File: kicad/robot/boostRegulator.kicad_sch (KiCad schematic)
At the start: 22 parts, among them U5 LSF0102DCTR, U6 MAX77857

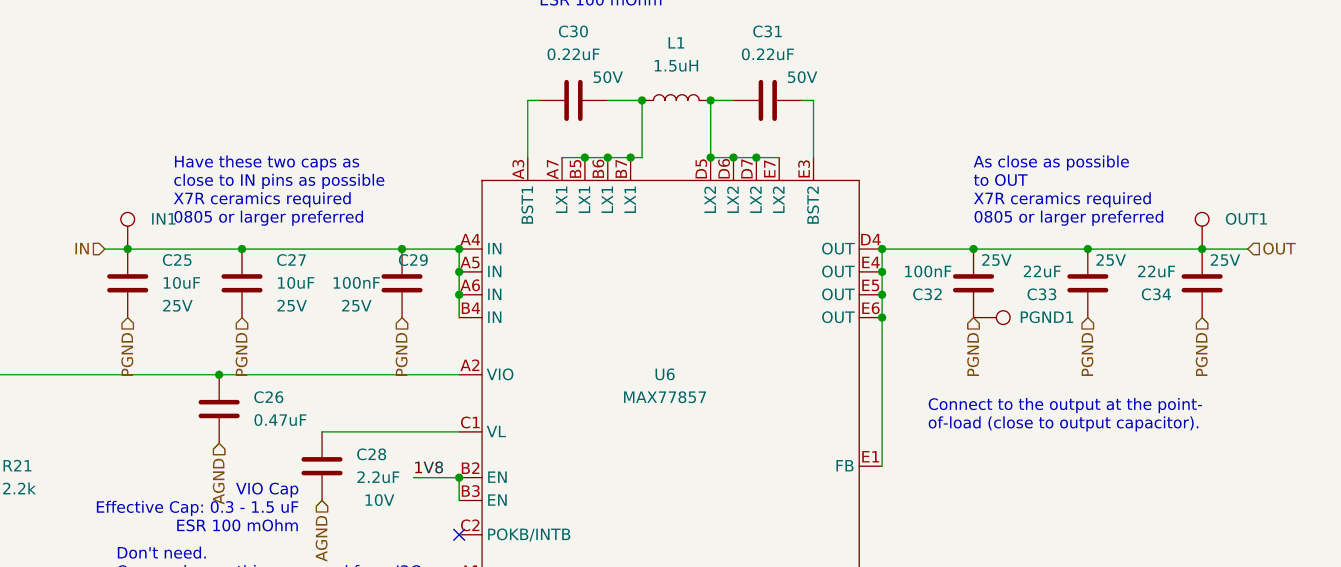
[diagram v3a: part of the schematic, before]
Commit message: Assigned capacitor footprints
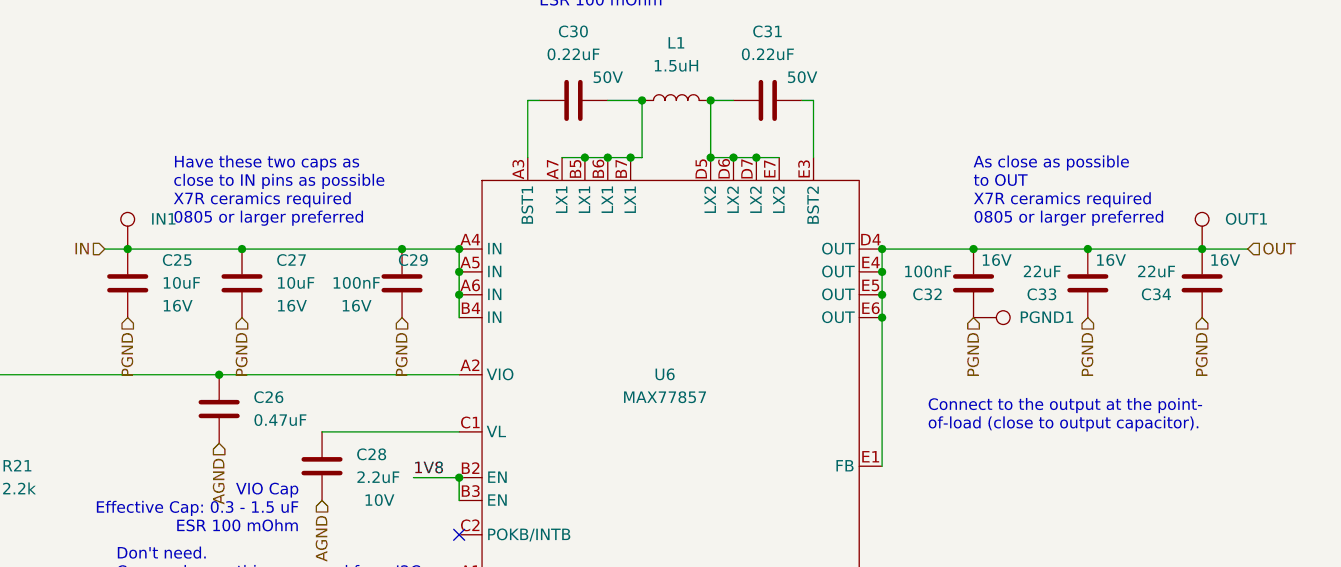
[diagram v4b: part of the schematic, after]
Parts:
- C24, C26, C28, C30, C31: footprint (none) -> Capacitor_SMD:C_0603_1608Metric
- C25, C27, C29, C32, C33, C34: footprint (none) -> Capacitor_SMD:C_0805_2012Metric
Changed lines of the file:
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@@
       (effects (font (size 1.27 1.27)) (justify left))
     )
-    (property "Footprint" "" (id 2) (at 157.1752 118.11 0)
+    (property "Footprint" "Capacitor_SMD:C_0603_1608Metric" (id 2) (at 157.1752 118.11 0)
       (effects (font (size 1.27 1.27)) hide)
     )
@@
     (property "Reference" "C32" (id 0) (at 223.52 95.25 0))
     (property "Value" "100nF" (id 1) (at 223.52 92.71 0))
-    (property "Footprint" "" (id 2) (at 227.6348 90.17 0)
+    (property "Footprint" "Capacitor_SMD:C_0805_2012Metric" (id 2) (at 227.6348 90.17 0)
       (effects (font (size 1.27 1.27)) hide)
     )
@@
       (effects (font (size 1.27 1.27)) hide)
     )
-    (property "Description" "25V" (id 4) (at 231.14 91.44 0))
+    (property "Description" "16V" (id 4) (at 231.14 91.44 0))
     (pin "1")
     (pin "2")
@@
       (effects (font (size 1.27 1.27)) (justify left))
     )
-    (property "Footprint" "" (id 2) (at 148.2852 97.79 0)
+    (property "Footprint" "Capacitor_SMD:C_0805_2012Metric" (id 2) (at 148.2852 97.79 0)
       (effects (font (size 1.27 1.27)) hide)
     )
@@
       (effects (font (size 1.27 1.27)) hide)
     )
-    (property "Description" "25V" (id 4) (at 151.13 96.5199 0)
+    (property "Description" "16V" (id 4) (at 151.13 96.5199 0)
       (effects (font (size 1.27 1.27)) (justify left))
     )
@@
       (effects (font (size 1.27 1.27)) (justify left))
     )
-    (property "Footprint" "" (id 2) (at 135.5852 97.79 0)
+    (property "Footprint" "Capacitor_SMD:C_0805_2012Metric" (id 2) (at 135.5852 97.79 0)
       (effects (font (size 1.27 1.27)) hide)
     )
@@
       (effects (font (size 1.27 1.27)) hide)
     )
-    (property "Description" "25V" (id 4) (at 138.43 96.5199 0)
+    (property "Description" "16V" (id 4) (at 138.43 96.5199 0)
       (effects (font (size 1.27 1.27)) (justify left))
     )
@@
       (effects (font (size 1.27 1.27)) (justify left))
     )
-    (property "Footprint" "" (id 2) (at 45.4152 124.46 0)
+    (property "Footprint" "Capacitor_SMD:C_0603_1608Metric" (id 2) (at 45.4152 124.46 0)
       (effects (font (size 1.27 1.27)) hide)
     )
@@
     (property "Reference" "C29" (id 0) (at 166.37 91.44 0))
     (property "Value" "100nF" (id 1) (at 160.02 93.98 0))
-    (property "Footprint" "" (id 2) (at 164.1348 90.17 0)
+    (property "Footprint" "Capacitor_SMD:C_0805_2012Metric" (id 2) (at 164.1348 90.17 0)
       (effects (font (size 1.27 1.27)) hide)
     )
@@
       (effects (font (size 1.27 1.27)) hide)
     )
-    (property "Description" "25V" (id 4) (at 160.02 96.52 0))
+    (property "Description" "16V" (id 4) (at 160.02 96.52 0))
     (pin "1")
     (pin "2")
@@
     (property "Reference" "C34" (id 0) (at 248.92 95.25 0))
     (property "Value" "22uF" (id 1) (at 248.92 92.71 0))
-    (property "Footprint" "" (id 2) (at 253.0348 90.17 0)
+    (property "Footprint" "Capacitor_SMD:C_0805_2012Metric" (id 2) (at 253.0348 90.17 0)
       (effects (font (size 1.27 1.27)) hide)
     )
@@
       (effects (font (size 1.27 1.27)) hide)
     )
-    (property "Description" "25V" (id 4) (at 256.54 91.44 0))
+    (property "Description" "16V" (id 4) (at 256.54 91.44 0))
     (pin "1")
     (pin "2")
@@
     (property "Reference" "C33" (id 0) (at 236.22 95.25 0))
     (property "Value" "22uF" (id 1) (at 236.22 92.71 0))
-    (property "Footprint" "" (id 2) (at 240.3348 90.17 0)
+    (property "Footprint" "Capacitor_SMD:C_0805_2012Metric" (id 2) (at 240.3348 90.17 0)
       (effects (font (size 1.27 1.27)) hide)
     )
@@
       (effects (font (size 1.27 1.27)) hide)
     )
-    (property "Description" "25V" (id 4) (at 243.84 91.44 0))
+    (property "Description" "16V" (id 4) (at 243.84 91.44 0))
     (pin "1")
     (pin "2")
@@
     (property "Reference" "C30" (id 0) (at 184.15 66.04 90))
     (property "Value" "0.22uF" (id 1) (at 184.15 68.58 90))
-    (property "Footprint" "" (id 2) (at 187.96 72.6948 0)
+    (property "Footprint" "Capacitor_SMD:C_0603_1608Metric" (id 2) (at 187.96 72.6948 0)
       (effects (font (size 1.27 1.27)) hide)
     )
@@
       (effects (font (size 1.27 1.27)) (justify left))
     )
-    (property "Footprint" "" (id 2) (at 145.7452 111.76 0)
+    (property "Footprint" "Capacitor_SMD:C_0603_1608Metric" (id 2) (at 145.7452 111.76 0)
       (effects (font (size 1.27 1.27)) hide)
     )
@@
     (property "Reference" "C31" (id 0) (at 205.74 66.04 90))
     (property "Value" "0.22uF" (id 1) (at 205.74 68.58 90))
-    (property "Footprint" "" (id 2) (at 209.55 72.6948 0)
-      (effects (font (size 1.27 1.27)) hide)
-    )
+    (property "Footprint" "Capacitor_SMD:C_0603_1608Metric" (id 2) (at 209.55 72.6948 0)
+      (effects (font (size 1.27 1.27)) hide)
+    )

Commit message: Added IND_TAIYO_NRS6028_TAY footprint and model to boost
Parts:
- L1: footprint (none) -> custom_inductors:NRS6028T1R5NMGJ; Manufacturer (none) -> TAIYO YUDEN; Part Number CDMT40D20HF-1R5NC -> NRS6028T1R5NMGJ
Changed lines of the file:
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@@
     (property "Reference" "L1" (id 0) (at 195.58 67.31 90))
     (property "Value" "1.5uH" (id 1) (at 195.58 69.85 90))
-    (property "Footprint" "" (id 2) (at 195.58 73.66 0)
+    (property "Footprint" "custom_inductors:NRS6028T1R5NMGJ" (id 2) (at 195.58 73.66 0)
       (effects (font (size 1.27 1.27)) hide)
     )
-    (property "Datasheet" "~" (id 3) (at 195.58 73.66 0)
+    (property "Datasheet" "https://www.mouser.jp/datasheet/2/396/wound04_e-1290968.pdf" (id 3) (at 195.58 73.66 0)
       (effects (font (size 1.27 1.27)) hide)
     )
-    (property "Part Number" "CDMT40D20HF-1R5NC" (id 4) (at 195.58 73.66 0)
+    (property "Part Number" "NRS6028T1R5NMGJ" (id 4) (at 195.58 73.66 0)
       (effects (font (size 1.27 1.27)) hide)
     )
-    (property "Description" "DCR < 22 mOhms. I_sat > 7A" (id 5) (at 195.58 73.66 0)
+    (property "Description" "DCR < 22 mOhms. I_sat > 4A" (id 5) (at 195.58 73.66 0)
       (effects (font (size 1.27 1.27)) hide)
     )
+    (property "Manufacturer" "TAIYO YUDEN" (id 6) (at 195.58 73.66 0)
+      (effects (font (size 1.27 1.27)) hide)
+    )

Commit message: Added keystone test points
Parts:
- IN1, OUT1, PGND1, SCL1V1, SDA1V1: footprint (none) -> TestPoint:KEYSTONE_5002
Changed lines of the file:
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@@
       (effects (font (size 1.27 1.27)) (justify left) hide)
     )
-    (property "Footprint" "" (id 2) (at 139.7 90.17 0)
+    (property "Footprint" "TestPoint:KEYSTONE_5002" (id 2) (at 139.7 90.17 0)
       (effects (font (size 1.27 1.27)) hide)
     )
@@
       (effects (font (size 1.27 1.27)) (justify left) hide)
     )
-    (property "Footprint" "" (id 2) (at 101.6 129.54 0)
+    (property "Footprint" "TestPoint:KEYSTONE_5002" (id 2) (at 101.6 129.54 0)
       (effects (font (size 1.27 1.27)) hide)
     )
@@
       (effects (font (size 1.27 1.27)) (justify left) hide)
     )
-    (property "Footprint" "" (id 2) (at 259.08 90.17 0)
+    (property "Footprint" "TestPoint:KEYSTONE_5002" (id 2) (at 259.08 90.17 0)
       (effects (font (size 1.27 1.27)) hide)
     )
@@
       (effects (font (size 1.27 1.27)) (justify left) hide)
     )
-    (property "Footprint" "" (id 2) (at 228.6 102.87 0)
+    (property "Footprint" "TestPoint:KEYSTONE_5002" (id 2) (at 228.6 102.87 0)
       (effects (font (size 1.27 1.27)) hide)
     )
@@
       (effects (font (size 1.27 1.27)) (justify left) hide)
     )
-    (property "Footprint" "" (id 2) (at 101.6 127 0)
-      (effects (font (size 1.27 1.27)) hide)
-    )
+    (property "Footprint" "TestPoint:KEYSTONE_5002" (id 2) (at 101.6 127 0)
+      (effects (font (size 1.27 1.27)) hide)
+    )

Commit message: WARNING Major BOM cleanup
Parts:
- TP31: renamed from SCL1V1; value TestPoint -> TP5002
- TP32: renamed from SDA1V1; value TestPoint -> TP5002
- TP33: renamed from PGND1; value TestPoint -> TP5002
- TP34: renamed from OUT1; value TestPoint -> TP5002
- TP36: renamed from IN1; value TestPoint -> TP5002
- U5: MANUFACTURER Texas Instruments -> (none); Manufacturer (none) -> Texas Instruments
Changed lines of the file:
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@@
   (symbol (lib_id "Connector:TestPoint") (at 134.62 90.17 0) (unit 1)
     (in_bom yes) (on_board yes) (fields_autoplaced)
-    (property "Reference" "IN1" (id 0) (at 137.16 86.8679 0)
-      (effects (font (size 1.27 1.27)) (justify left))
-    )
-    (property "Value" "TestPoint" (id 1) (at 137.16 88.1379 0)
+    (property "Reference" "TP36" (id 0) (at 137.16 86.8679 0)
+      (effects (font (size 1.27 1.27)) (justify left))
+    )
+    (property "Value" "TP5002" (id 1) (at 137.16 88.1379 0)
       (effects (font (size 1.27 1.27)) (justify left) hide)
     )
@@
       (effects (font (size 1.27 1.27)) (justify left bottom) hide)
     )
-    (property "MANUFACTURER" "Texas Instruments" (id 6) (at 78.74 127 0)
+    (property "MANUFACTURER" "" (id 6) (at 78.74 127 0)
       (effects (font (size 1.27 1.27)) (justify left bottom) hide)
     )
     (property "MAXIMUM_PACKAGE_HEIGHT" "1.3 mm" (id 7) (at 78.74 127 0)
       (effects (font (size 1.27 1.27)) (justify left bottom) hide)
+    )
+    (property "Manufacturer" "Texas Instruments" (id 8) (at 78.74 127 0)
+      (effects (font (size 1.27 1.27)) hide)
     )
     (pin "1")
@@
   (symbol (lib_id "Connector:TestPoint") (at 96.52 129.54 0) (mirror x) (unit 1)
     (in_bom yes) (on_board yes)
-    (property "Reference" "SDA1V1" (id 0) (at 106.68 133.35 0)
+    (property "Reference" "TP32" (id 0) (at 102.87 134.62 0)
       (effects (font (size 1.27 1.27)) (justify right))
     )
-    (property "Value" "TestPoint" (id 1) (at 99.06 131.5721 0)
+    (property "Value" "TP5002" (id 1) (at 99.06 131.5721 0)
       (effects (font (size 1.27 1.27)) (justify left) hide)
     )
@@
       (effects (font (size 1.27 1.27)) hide)
     )
+    (property "Description" "SDA1V1" (id 4) (at 96.52 129.54 0)
+      (effects (font (size 1.27 1.27)) hide)
+    )
     (pin "1")
   )
   (symbol (lib_id "Connector:TestPoint") (at 254 90.17 0) (unit 1)
     (in_bom yes) (on_board yes) (fields_autoplaced)
-    (property "Reference" "OUT1" (id 0) (at 256.54 86.8679 0)
-      (effects (font (size 1.27 1.27)) (justify left))
-    )
-    (property "Value" "TestPoint" (id 1) (at 256.54 88.1379 0)
+    (property "Reference" "TP34" (id 0) (at 256.54 86.8679 0)
+      (effects (font (size 1.27 1.27)) (justify left))
+    )
+    (property "Value" "TP5002" (id 1) (at 256.54 88.1379 0)
       (effects (font (size 1.27 1.27)) (justify left) hide)
     )
@@
       (effects (font (size 1.27 1.27)) hide)
     )
+    (property "Description" "OUT" (id 4) (at 254 90.17 0)
+      (effects (font (size 1.27 1.27)) hide)
+    )
     (pin "1")
   )
   (symbol (lib_id "Connector:TestPoint") (at 228.6 97.79 270) (unit 1)
     (in_bom yes) (on_board yes) (fields_autoplaced)
-    (property "Reference" "PGND1" (id 0) (at 233.68 97.7899 90)
-      (effects (font (size 1.27 1.27)) (justify left))
-    )
-    (property "Value" "TestPoint" (id 1) (at 230.6321 100.33 0)
+    (property "Reference" "TP33" (id 0) (at 233.68 97.7899 90)
+      (effects (font (size 1.27 1.27)) (justify left))
+    )
+    (property "Value" "TP5002" (id 1) (at 230.6321 100.33 0)
       (effects (font (size 1.27 1.27)) (justify left) hide)
     )
@@
     )
     (property "Datasheet" "~" (id 3) (at 228.6 102.87 0)
+      (effects (font (size 1.27 1.27)) hide)
+    )
+    (property "Description" "PGND" (id 4) (at 228.6 97.79 0)
       (effects (font (size 1.27 1.27)) hide)
     )
@@
   (symbol (lib_id "Connector:TestPoint") (at 96.52 127 0) (unit 1)
     (in_bom yes) (on_board yes) (fields_autoplaced)
-    (property "Reference" "SCL1V1" (id 0) (at 99.06 123.6979 0)
-      (effects (font (size 1.27 1.27)) (justify left))
-    )
-    (property "Value" "TestPoint" (id 1) (at 99.06 124.9679 0)
+    (property "Reference" "TP31" (id 0) (at 99.06 123.6979 0)
+      (effects (font (size 1.27 1.27)) (justify left))
+    )
+    (property "Value" "TP5002" (id 1) (at 99.06 124.9679 0)
       (effects (font (size 1.27 1.27)) (justify left) hide)
     )
@@
       (effects (font (size 1.27 1.27)) hide)
     )
+    (property "Description" "SCL1V1" (id 4) (at 96.52 127 0)
+      (effects (font (size 1.27 1.27)) hide)
+    )

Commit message: WARNING more BOM batch edits
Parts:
- TP31, TP32, TP33, TP34, TP36: Manufacturer (none) -> Keystone Electronics; Part Number (none) -> 5002
- U5: Part Number (none) -> LSF0102DCTR
- U6: Part Number (none) -> MAX77857
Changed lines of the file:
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@@
+      (effects (font (size 1.27 1.27)) hide)
+    )
+    (property "Part Number" "MAX77857" (id 4) (at 194.31 106.68 0)
       (effects (font (size 1.27 1.27)) hide)
     )
@@
       (effects (font (size 1.27 1.27)) hide)
     )
+    (property "Manufacturer" "Keystone Electronics" (id 4) (at 134.62 90.17 0)
+      (effects (font (size 1.27 1.27)) hide)
+    )
+    (property "Part Number" "5002" (id 5) (at 134.62 90.17 0)
+      (effects (font (size 1.27 1.27)) hide)
+    )
     (pin "1")
   )
@@
     )
     (property "Manufacturer" "Texas Instruments" (id 8) (at 78.74 127 0)
+      (effects (font (size 1.27 1.27)) hide)
+    )
+    (property "Part Number" "LSF0102DCTR" (id 9) (at 78.74 127 0)
       (effects (font (size 1.27 1.27)) hide)
     )
@@
       (effects (font (size 1.27 1.27)) hide)
     )
+    (property "Manufacturer" "Keystone Electronics" (id 5) (at 96.52 129.54 0)
+      (effects (font (size 1.27 1.27)) hide)
+    )
+    (property "Part Number" "5002" (id 6) (at 96.52 129.54 0)
+      (effects (font (size 1.27 1.27)) hide)
+    )
     (pin "1")
   )
@@
       (effects (font (size 1.27 1.27)) hide)
     )
+    (property "Manufacturer" "Keystone Electronics" (id 5) (at 254 90.17 0)
+      (effects (font (size 1.27 1.27)) hide)
+    )
+    (property "Part Number" "5002" (id 6) (at 254 90.17 0)
+      (effects (font (size 1.27 1.27)) hide)
+    )
     (pin "1")
   )
@@
     )
     (property "Description" "PGND" (id 4) (at 228.6 97.79 0)
+      (effects (font (size 1.27 1.27)) hide)
+    )
+    (property "Manufacturer" "Keystone Electronics" (id 5) (at 228.6 97.79 0)
+      (effects (font (size 1.27 1.27)) hide)
+    )
+    (property "Part Number" "5002" (id 6) (at 228.6 97.79 0)
       (effects (font (size 1.27 1.27)) hide)
     )
@@
       (effects (font (size 1.27 1.27)) hide)
     )
+    (property "Manufacturer" "Keystone Electronics" (id 5) (at 96.52 127 0)
+      (effects (font (size 1.27 1.27)) hide)
+    )
+    (property "Part Number" "5002" (id 6) (at 96.52 127 0)
+      (effects (font (size 1.27 1.27)) hide)
+    )
